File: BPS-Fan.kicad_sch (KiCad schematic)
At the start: 33 parts, among them J1 LDRBRDConn, J10 FAN9, J11 FAN10, J12 FAN11, J13 FAN12, J2 FAN1, J3 FAN2, J4 FAN3, J5 FAN4, J6 FAN5, J7 FAN6, J8 FAN7, J9 FAN8, Q1 BUK9M23-80E, Q10 BUK9M23-80E, Q4 BUK9M23-80E, Q7 BUK9M23-80E

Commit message: Added PUR
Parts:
- gave numbers to parts that had none: 4
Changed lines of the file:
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@@
   (symbol (lib_id "Device:R") (at 33.02 144.78 0) (unit 1)
     (in_bom yes) (on_board yes) (fields_autoplaced)
-    (property "Reference" "R?" (id 0) (at 35.56 143.5099 0)
+    (property "Reference" "R2" (id 0) (at 35.56 143.5099 0)
       (effects (font (size 1.27 1.27)) (justify left))
     )
@@
   (symbol (lib_id "Device:R") (at 194.31 110.49 0) (unit 1)
     (in_bom yes) (on_board yes) (fields_autoplaced)
-    (property "Reference" "R?" (id 0) (at 196.85 109.2199 0)
+    (property "Reference" "R5" (id 0) (at 196.85 109.2199 0)
       (effects (font (size 1.27 1.27)) (justify left))
     )
@@
   (symbol (lib_id "Device:R") (at 116.84 162.56 0) (unit 1)
     (in_bom yes) (on_board yes) (fields_autoplaced)
-    (property "Reference" "R?" (id 0) (at 119.38 161.2899 0)
+    (property "Reference" "R3" (id 0) (at 119.38 161.2899 0)
       (effects (font (size 1.27 1.27)) (justify left))
     )
@@
   (symbol (lib_id "Device:R") (at 121.92 91.44 0) (unit 1)
     (in_bom yes) (on_board yes) (fields_autoplaced)
-    (property "Reference" "R?" (id 0) (at 124.46 90.1699 0)
+    (property "Reference" "R4" (id 0) (at 124.46 90.1699 0)
       (effects (font (size 1.27 1.27)) (justify left))
     )
@@
     )
     (path "/05545c6b-36f6-4a81-952c-42dacce1cfc6"
-      (reference "R?") (unit 1) (value "100k") (footprint "Resistor_SMD:R_0805_2012Metric")
+      (reference "R2") (unit 1) (value "100k") (footprint "Resistor_SMD:R_0805_2012Metric")
+    )
+    (path "/4b907299-6873-4907-adaf-4f73f43d3a9c"
+      (reference "R3") (unit 1) (value "100k") (footprint "Resistor_SMD:R_0805_2012Metric")
+    )
+    (path "/b52066d7-4d36-48f0-a722-893d718b5089"
+      (reference "R4") (unit 1) (value "100k") (footprint "Resistor_SMD:R_0805_2012Metric")
     )
     (path "/2efcbd77-bd5c-4085-acee-b1ecf99eb7c8"
-      (reference "R?") (unit 1) (value "100k") (footprint "Resistor_SMD:R_0805_2012Metric")
-    )
-    (path "/4b907299-6873-4907-adaf-4f73f43d3a9c"
-      (reference "R?") (unit 1) (value "100k") (footprint "Resistor_SMD:R_0805_2012Metric")
-    )
-    (path "/b52066d7-4d36-48f0-a722-893d718b5089"
-      (reference "R?") (unit 1) (value "100k") (footprint "Resistor_SMD:R_0805_2012Metric")
-    )
-  )
+      (reference "R5") (unit 1) (value "100k") (footprint "Resistor_SMD:R_0805_2012Metric")
+    )
+  )

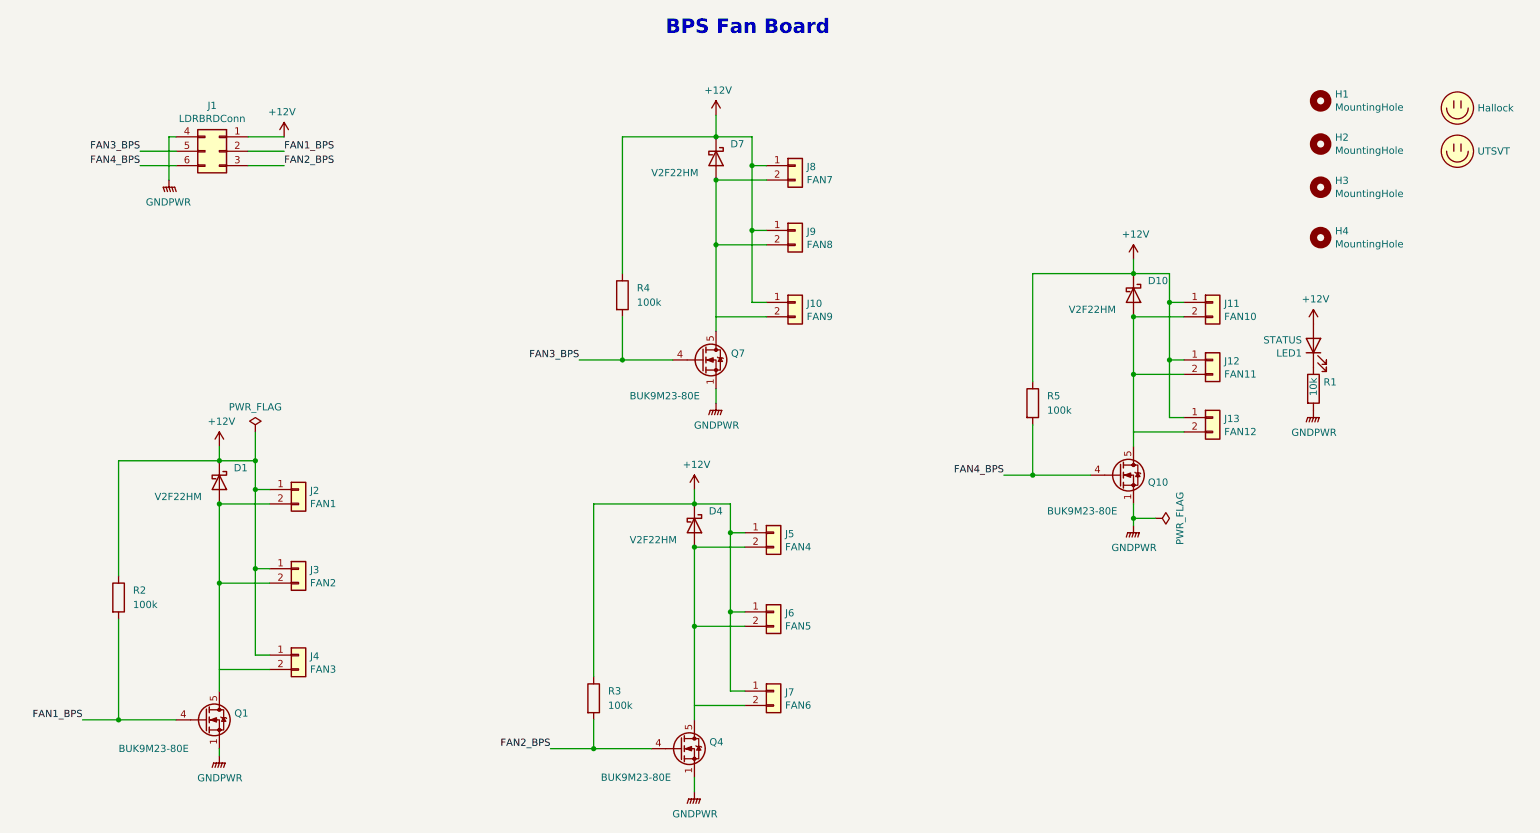
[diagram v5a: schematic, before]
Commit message: preliminary idea for layout, NOT cleaned up yet!
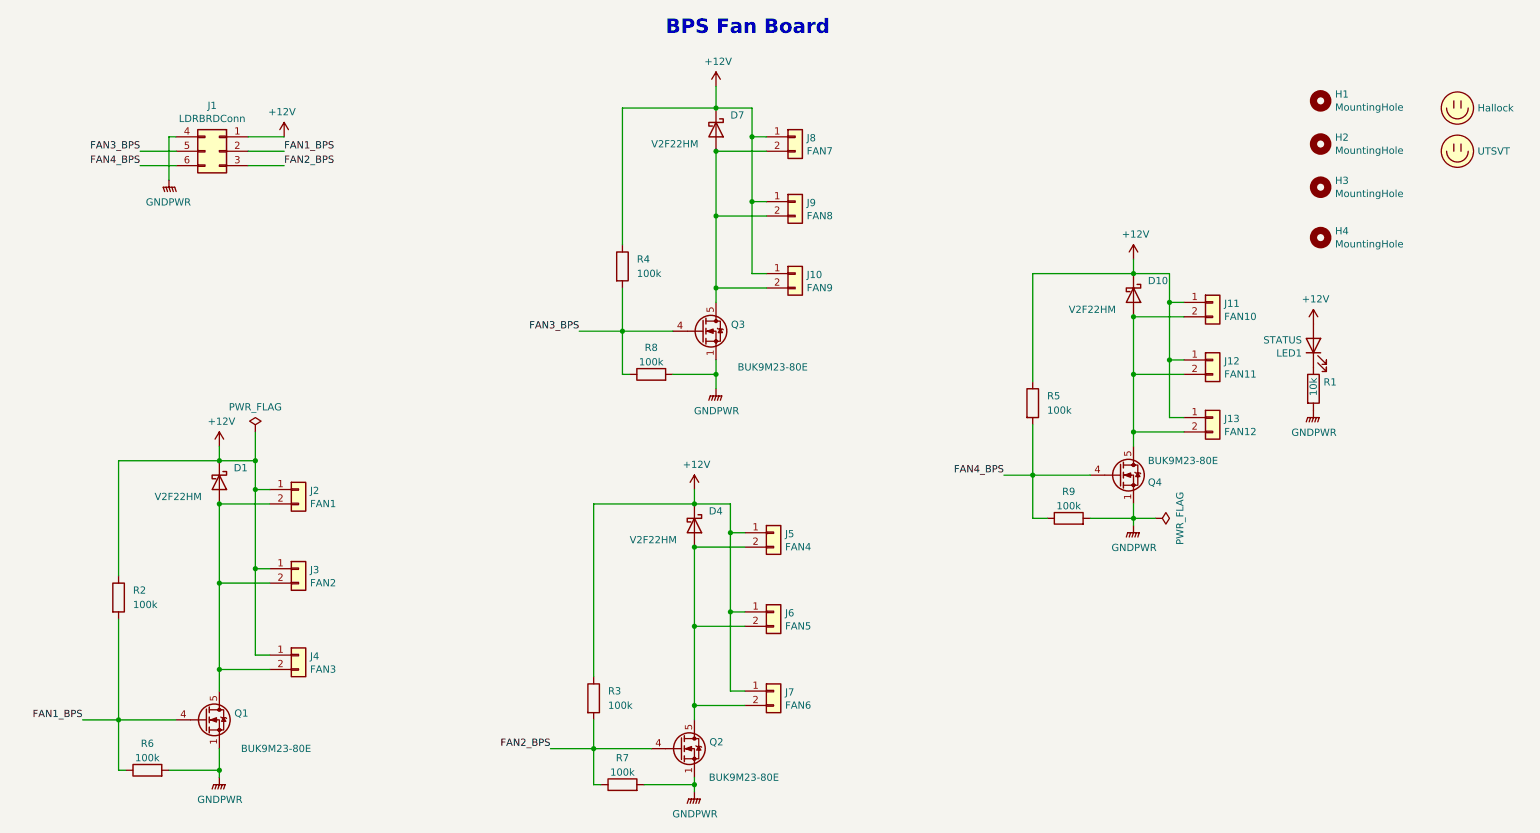
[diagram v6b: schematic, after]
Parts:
- added R6, R7, R8, R9: 100k, Resistor_SMD:R_0805_2012Metric, symbol Device:R
- renumbered Q4 to Q2, Q7 to Q3, Q10 to Q4
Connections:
- net FAN1_BPS: now also R6.1
- net FAN2_BPS: now also R7.1
- net FAN3_BPS: now also R8.1
- net FAN4_BPS: now also R9.1
- net GNDPWR: now also R6.2, R7.2, R8.2, R9.2
- net at D10.2 (A), J11.2 (Pin_2), J12.2 (Pin_2)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: now also J13.2 (Pin_2)
- net at D1.2 (A), J2.2 (Pin_2), J3.2 (Pin_2)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: now also J4.2 (Pin_2)
- net at J7.2 (Pin_2): now also D4.2 (A), J5.2 (Pin_2), J6.2 (Pin_2), Q2.5 (D)
- net at D7.2 (A), J8.2 (Pin_2), J9.2 (Pin_2)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: now also J10.2 (Pin_2)
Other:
- moved on the sheet: D7, J10, J8, J9, Q3, R4

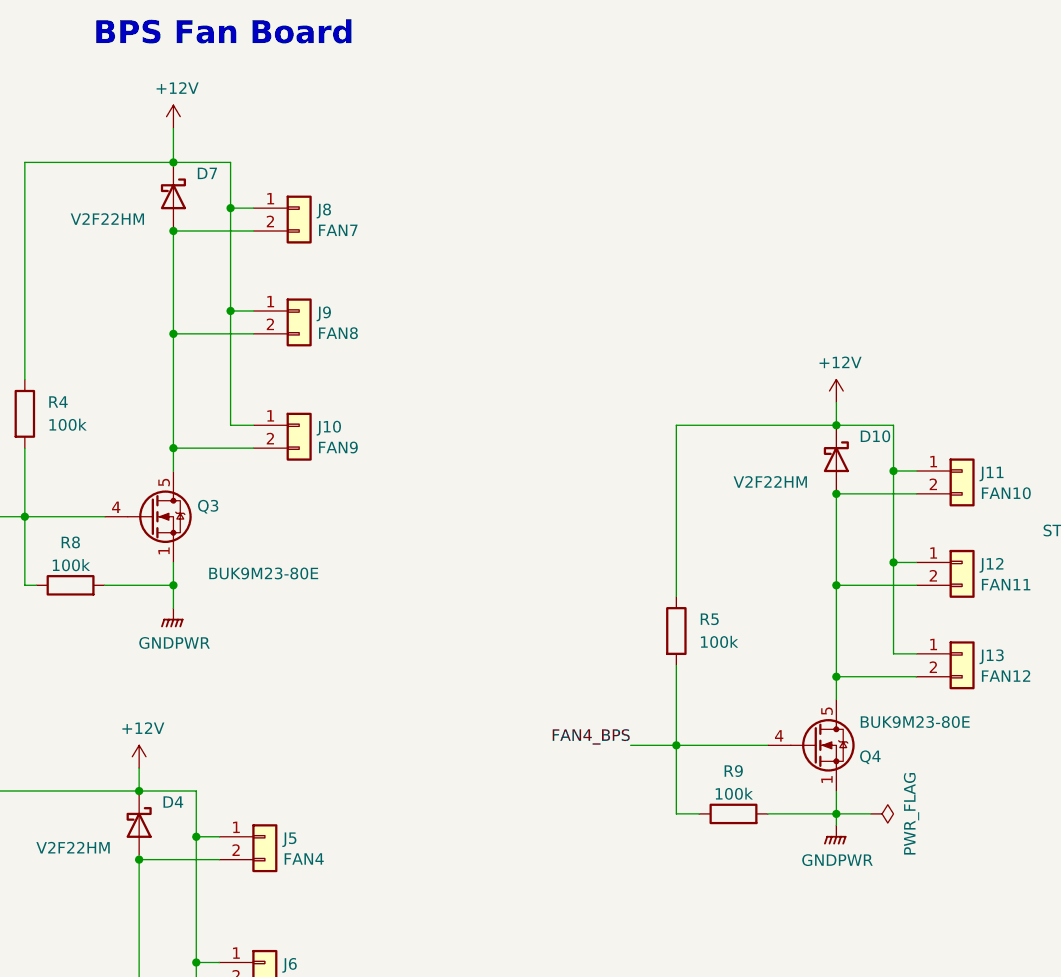
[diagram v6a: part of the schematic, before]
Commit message: Complete layout of fan board
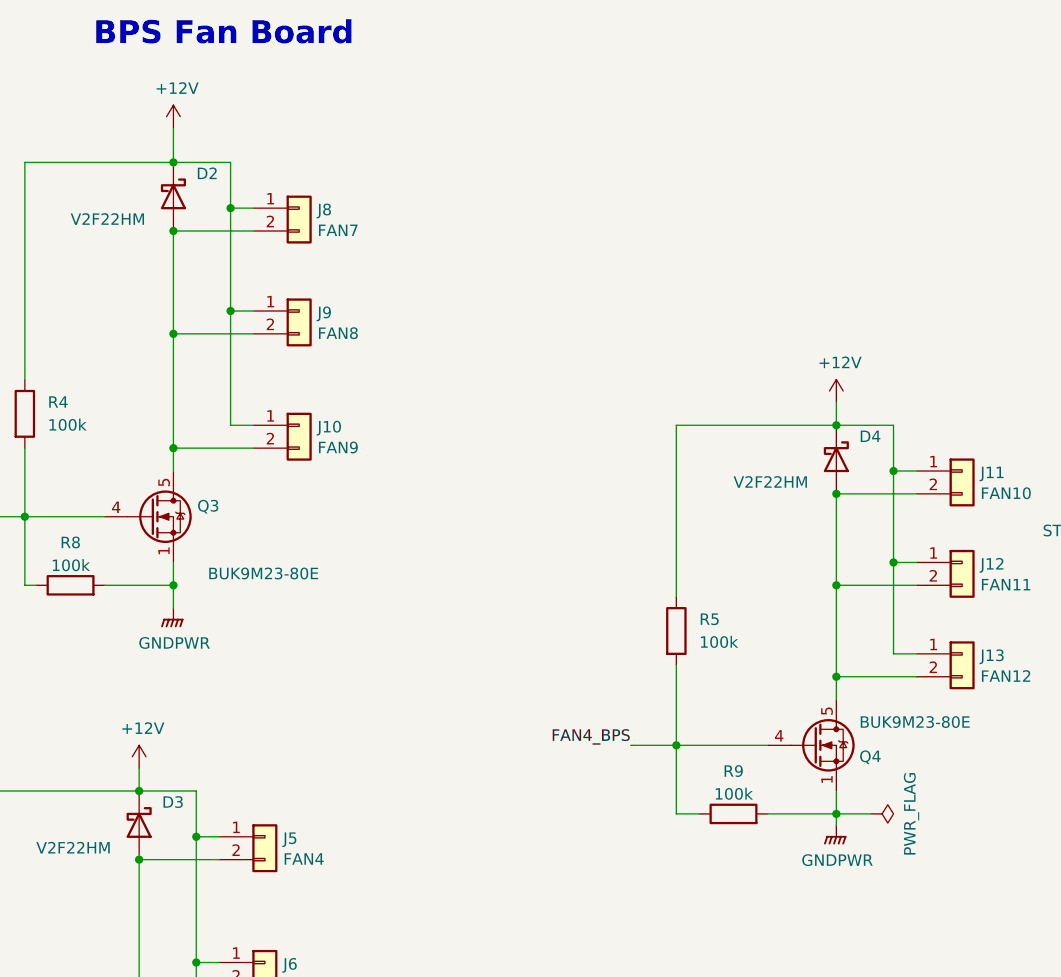
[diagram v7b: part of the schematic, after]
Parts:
- renumbered D7 to D2, D4 to D3, D10 to D4
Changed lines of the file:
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@@
   (symbol (lib_id "Diode:C3D25170H") (at 212.09 91.44 270) (unit 1)
     (in_bom yes) (on_board yes)
-    (property "Reference" "D10" (id 0) (at 214.63 88.9 90)
+    (property "Reference" "D4" (id 0) (at 214.63 88.9 90)
       (effects (font (size 1.27 1.27)) (justify left))
     )
@@
   (symbol (lib_id "Diode:C3D25170H") (at 138.43 62.23 270) (unit 1)
     (in_bom yes) (on_board yes)
-    (property "Reference" "D7" (id 0) (at 140.97 59.69 90)
+    (property "Reference" "D2" (id 0) (at 140.97 59.69 90)
       (effects (font (size 1.27 1.27)) (justify left))
     )
@@
   (symbol (lib_id "Diode:C3D25170H") (at 134.62 132.08 270) (unit 1)
     (in_bom yes) (on_board yes)
-    (property "Reference" "D4" (id 0) (at 137.16 129.54 90)
+    (property "Reference" "D3" (id 0) (at 137.16 129.54 90)
       (effects (font (size 1.27 1.27)) (justify left))
     )
@@
       (reference "D1") (unit 1) (value "V2F22HM") (footprint "UTSVT_Passive:V2F22HM")
     )
+    (path "/996439a0-9ad5-4024-a65c-42386d89db2a"
+      (reference "D2") (unit 1) (value "V2F22HM") (footprint "UTSVT_Passive:V2F22HM")
+    )
     (path "/d94c94ed-42ff-4e7f-879f-801eb909b803"
+      (reference "D3") (unit 1) (value "V2F22HM") (footprint "UTSVT_Passive:V2F22HM")
+    )
+    (path "/097164b0-78ef-49b4-83cc-2fbdd82cec8a"
       (reference "D4") (unit 1) (value "V2F22HM") (footprint "UTSVT_Passive:V2F22HM")
     )
-    (path "/996439a0-9ad5-4024-a65c-42386d89db2a"
-      (reference "D7") (unit 1) (value "V2F22HM") (footprint "UTSVT_Passive:V2F22HM")
-    )
-    (path "/097164b0-78ef-49b4-83cc-2fbdd82cec8a"
-      (reference "D10") (unit 1) (value "V2F22HM") (footprint "UTSVT_Passive:V2F22HM")
-    )
     (path "/00000000-0000-0000-0000-00005f1dfa7f"

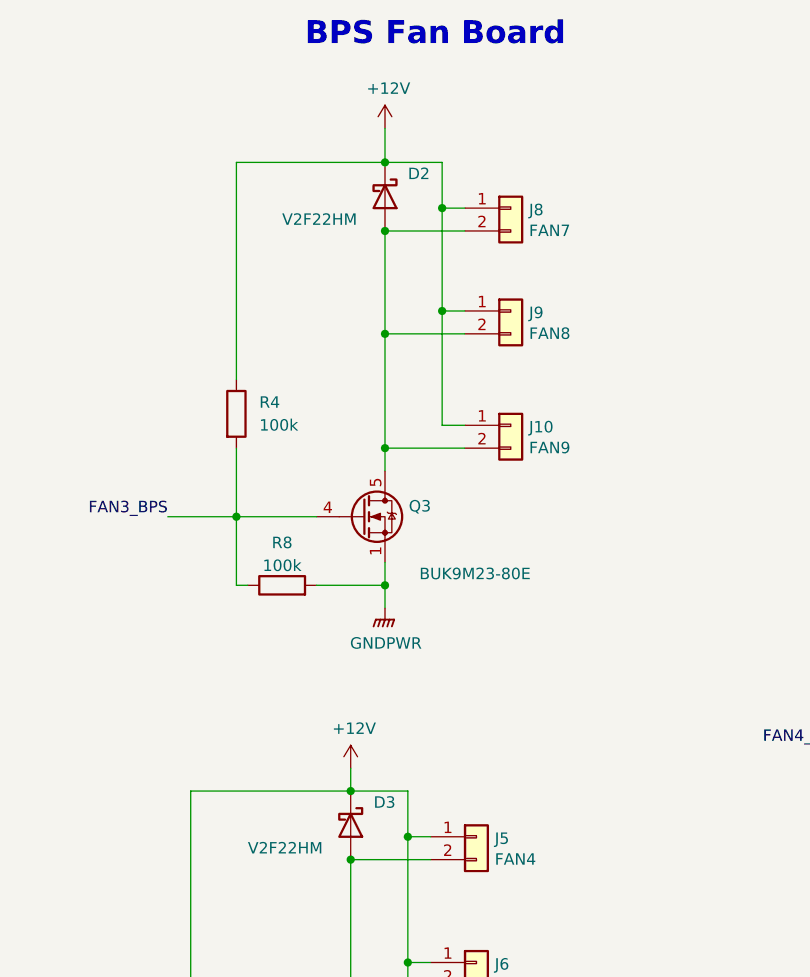
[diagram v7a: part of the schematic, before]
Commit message: added space between connectors as suggested by Raymond
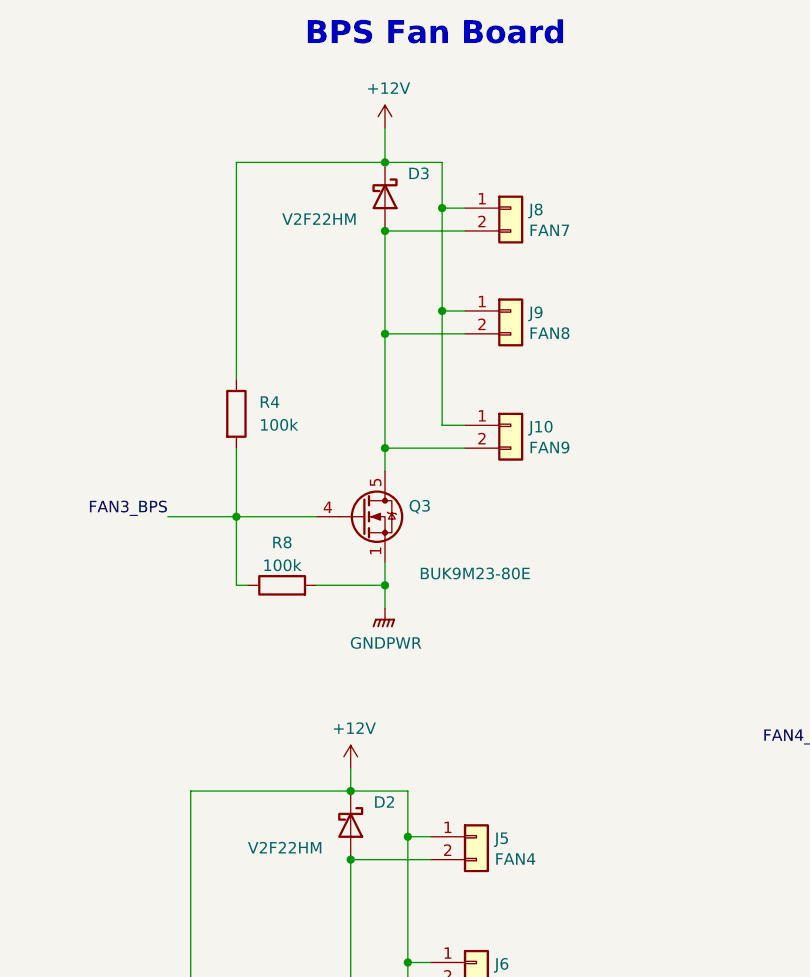
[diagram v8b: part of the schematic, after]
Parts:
- renumbered D3 to D2, D2 to D3
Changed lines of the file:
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@@
   (symbol (lib_id "Diode:C3D25170H") (at 138.43 62.23 270) (unit 1)
     (in_bom yes) (on_board yes)
-    (property "Reference" "D2" (id 0) (at 140.97 59.69 90)
+    (property "Reference" "D3" (id 0) (at 140.97 59.69 90)
       (effects (font (size 1.27 1.27)) (justify left))
     )
@@
   (symbol (lib_id "Diode:C3D25170H") (at 134.62 132.08 270) (unit 1)
     (in_bom yes) (on_board yes)
-    (property "Reference" "D3" (id 0) (at 137.16 129.54 90)
+    (property "Reference" "D2" (id 0) (at 137.16 129.54 90)
       (effects (font (size 1.27 1.27)) (justify left))
     )
@@
       (reference "D1") (unit 1) (value "V2F22HM") (footprint "UTSVT_Passive:V2F22HM")
     )
+    (path "/d94c94ed-42ff-4e7f-879f-801eb909b803"
+      (reference "D2") (unit 1) (value "V2F22HM") (footprint "UTSVT_Passive:V2F22HM")
+    )
     (path "/996439a0-9ad5-4024-a65c-42386d89db2a"
-      (reference "D2") (unit 1) (value "V2F22HM") (footprint "UTSVT_Passive:V2F22HM")
-    )
-    (path "/d94c94ed-42ff-4e7f-879f-801eb909b803"
       (reference "D3") (unit 1) (value "V2F22HM") (footprint "UTSVT_Passive:V2F22HM")
     )
